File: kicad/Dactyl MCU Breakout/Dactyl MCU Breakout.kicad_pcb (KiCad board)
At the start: 4 copper layers, 48.5 x 61.1 mm, 37 parts, among them J202 Split, J203 Column, J204 Thumb, J205 External, J206 Row, J207 Display, J208 Vic, J209 JST, SW201 Battery, SW202 Reset, SW203 LED, U201 SRV05-4, U202 Nice!Nano/2040

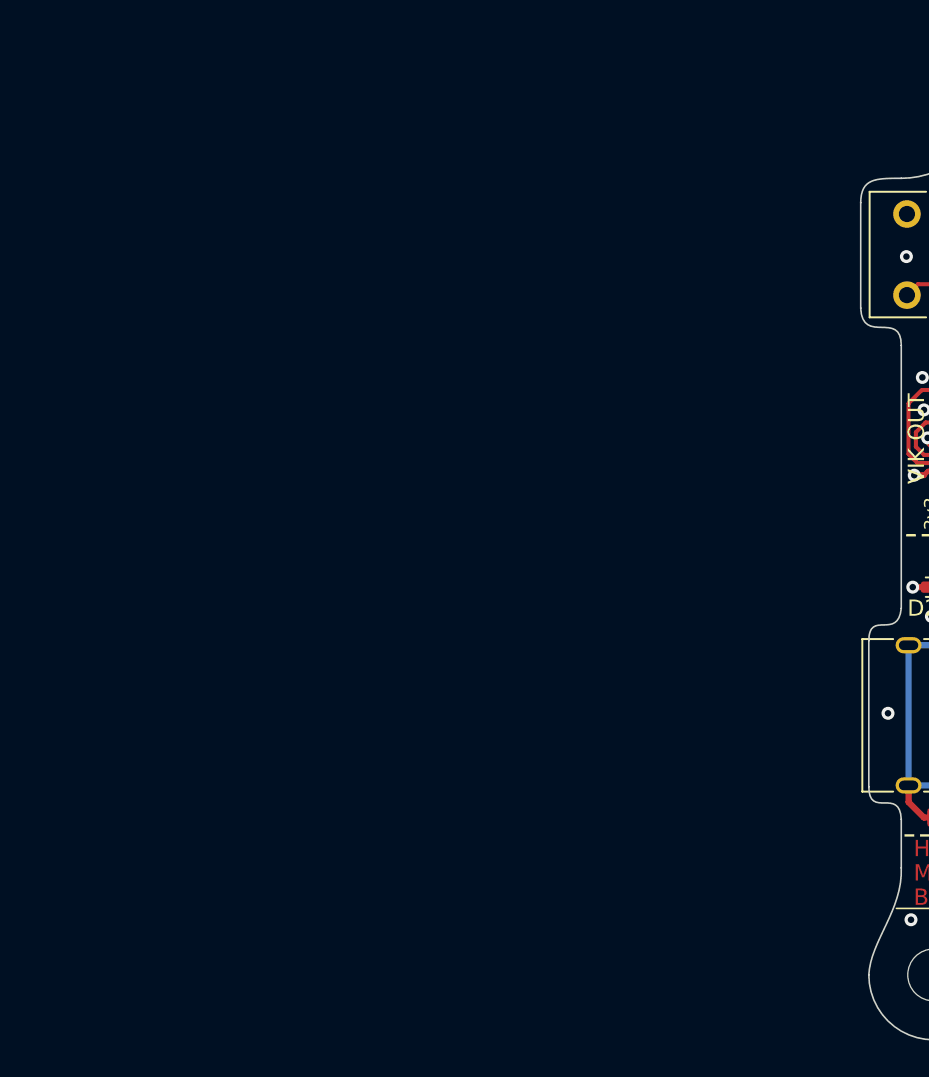
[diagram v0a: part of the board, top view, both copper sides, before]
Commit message: feat(pcb): mirror flipped
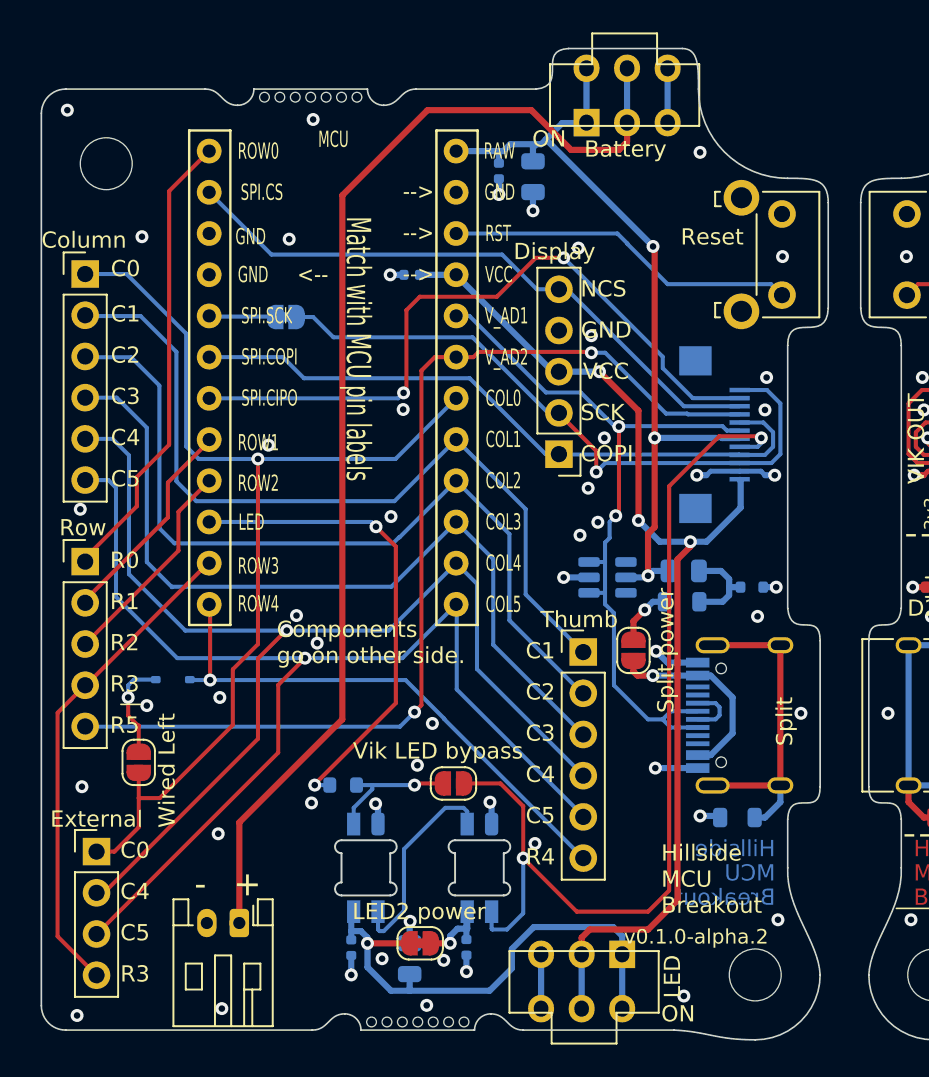
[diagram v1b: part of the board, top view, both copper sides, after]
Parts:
- added C202: 4.7uF, Capacitor_SMD:C_0805_2012Metric, B.Cu at (80.3, 55.4)
- added C203: 0.1uF, Capacitor_SMD:C_0402_1005Metric, B.Cu at (78.2, 55.0)
- added C204: 0.1uF, Capacitor_SMD:C_0402_1005Metric, B.Cu at (72.8, 61.5)
- added C205: 22uF, Capacitor_SMD:C_0805_2012Metric, B.Cu at (72.7, 103.6)
- added C206: 0.1uF, Capacitor_SMD:C_0402_1005Metric, B.Cu at (69.1, 102.9)
- added C207: 0.1uF, Capacitor_SMD:C_0402_1005Metric, B.Cu at (76.2, 102.9)
- added D201: ESD5Z5V0, Diode_SMD:D_SOD-523, B.Cu at (93.8, 80.7)
- added D202: D_Small, Diode_SMD:D_SOD-323, B.Cu at (58.1, 86.4)
- added D203: SK6812-MINI-E, Dactyl:SK6812-MINI-E-Dog2_1S, B.Cu at (70.0, 98.0)
- added D204: SK6812-MINI-E, Dactyl:SK6812-MINI-E-Dog2_1S, B.Cu at (77.0, 98.0)
- added F201: 750mA 6V Polyfuse, Fuse:Fuse_0805_2012Metric, B.Cu at (89.6, 79.7)
- added FB201: 20mΩ 100Ω@100MHz, Inductor_SMD:L_0805_2012Metric, B.Cu at (92.9, 94.9)
- added FB202: 20mΩ 100Ω@100MHz, Inductor_SMD:L_0805_2012Metric, B.Cu at (89.5, 81.6)
- added H201: MountingHole, Dactyl_basics:MountingHole_3.2mm_M3_DIN965, B.Cu at (54.0, 54.6)
- added H202: MountingHole, Dactyl_basics:MountingHole_3.2mm_M3_DIN965, B.Cu at (94.0, 104.6)
- added J202: Split, Dactyl_basics:USB_C_Receptacle_HRO_TYPE-C-31-M-12, B.Cu at (94.5, 88.6)
- added J203: Column, Dactyl:PinHeader_Columns, B.Cu at (52.7, 61.4)
- added J204: Thumb, Dactyl:PinHeader_Thumbs, B.Cu at (83.4, 84.7)
- added J205: External, Dactyl:PinHeader_External, B.Cu at (53.4, 97.0)
- added J206: Row, Dactyl:PinHeader_Rows, B.Cu at (52.7, 79.1)
- added J207: Display, Dactyl:PinHeader_Display, B.Cu at (81.9, 72.5)
- added J208: Vic, Dactyl:vik-keyboard-connector-horizontal, B.Cu at (91.0, 71.3)
- added J209: JST, Dactyl:JST_PH_S2B-PH-K_1x02_P2.00mm_Horizontal, B.Cu at (62.2, 101.4)
- added JP201: Split power, Dactyl_basics:SolderJumper-2_P1.3mm_Open_RoundedPad1.0x1.5mm, F.Cu at (86.5, 84.6)
- added JP202: Wired Left, Dactyl_basics:SolderJumper-2_P1.3mm_Open_RoundedPad1.0x1.5mm, F.Cu at (56.0, 91.5)
- added JP203: SCK term, Dactyl_basics:SolderJumper-2_P1.3mm_Bridged_RoundedPad1.0x1.5mm, B.Cu at (65.1, 64.0)
- added JP204: Vik LED bypass, Dactyl_basics:SolderJumper-2_P1.3mm_Open_RoundedPad1.0x1.5mm, F.Cu at (75.4, 92.8)
- added JP205: LED2 power, Dactyl_basics:SolderJumper-2_P1.3mm_Bridged_RoundedPad1.0x1.5mm, F.Cu at (73.3, 102.7)
- added R201: 300 Ohm, Resistor_SMD:R_0603_1608Metric, B.Cu at (68.6, 92.9)
- added REF**: art_name, Dactyl:art_name, B.Cu at (92.0, 98.4)
- added REF**: Mouse_Bites, Dactyl_basics:Mouse_Bites, B.Cu at (73.2, 107.5)
- added REF**: Mouse_Bites, Dactyl_basics:Mouse_Bites, B.Cu at (66.6, 50.5)
- added SW201: Battery, Dactyl:SW_SPDT_Battery, B.Cu at (86.1, 50.4)
- added SW202: Reset, Dactyl_basics:SW_Tactile_SKHL_Angled, B.Cu at (94.4, 60.2)
- added SW203: LED, Dactyl:SW_SPDT_JS202011AQN_wider, B.Cu at (83.3, 105.0)
- added U201: SRV05-4, Package_TO_SOT_SMD:SOT-23-6, B.Cu at (84.9, 80.1)
- added U202: Nice!Nano/2040, Dactyl:ProMicro_v2_1S, B.Cu at (68.0, 68.3)
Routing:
- net /Right/col4: track 71.4 -> 142.9 mm, vias 1 -> 2
- net /Right/col5: track 71.4 -> 142.8 mm, vias 1 -> 2
- net /Right/bat+: track 69.6 -> 139.2 mm
- net /Right/col0: track 64.5 -> 129.0 mm, vias 1 -> 2
- net /Right/VCC: track 64.1 -> 128.2 mm, vias 3 -> 6
- net /Right/row5_VIK_GP_AD2: track 63.6 -> 127.2 mm, vias 2 -> 4
- net /Right/LED_out: track 59.0 -> 118.0 mm, vias 2 -> 4
- net /Right/col2: track 50.8 -> 101.6 mm
- net /Right/col3: track 50.6 -> 101.1 mm
- net /Right/col1: track 50.2 -> 100.4 mm
- net /Right/RAW: track 48.5 -> 97.1 mm, vias 3 -> 6
- net /Right/SPLIT_VIK_GP_AD1: track 47.5 -> 95.1 mm, vias 2 -> 4
- net /Right/SPI0.CIPO: track 43.2 -> 86.3 mm, vias 2 -> 4
- net /Right/SPI0.SCK/SDA: track 41.0 -> 82.0 mm, vias 1 -> 2
- net /Right/SPI0.COPI/SCL: track 40.7 -> 81.4 mm
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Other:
- board size 48.5 x 61.1 mm -> 99 x 61.1 mm

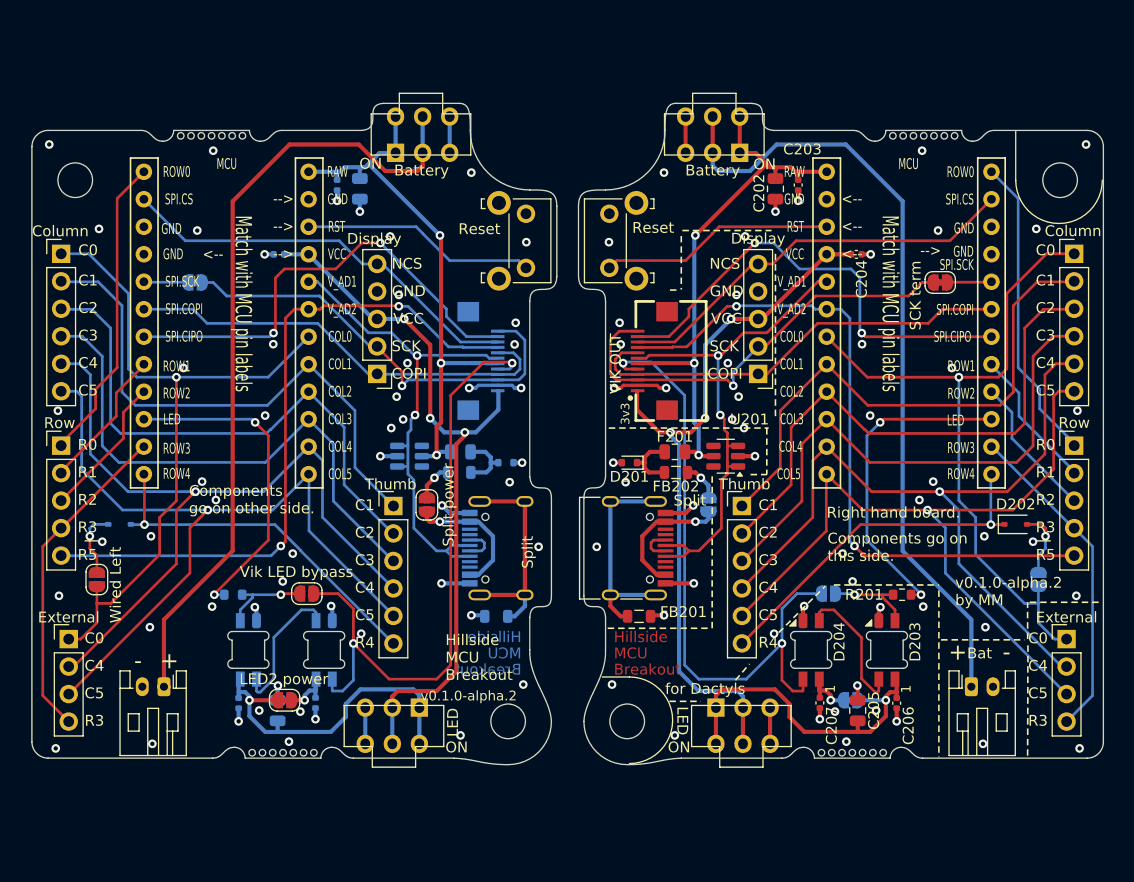
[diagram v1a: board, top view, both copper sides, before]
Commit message: feat(pcb): left half re-numbered and some routed
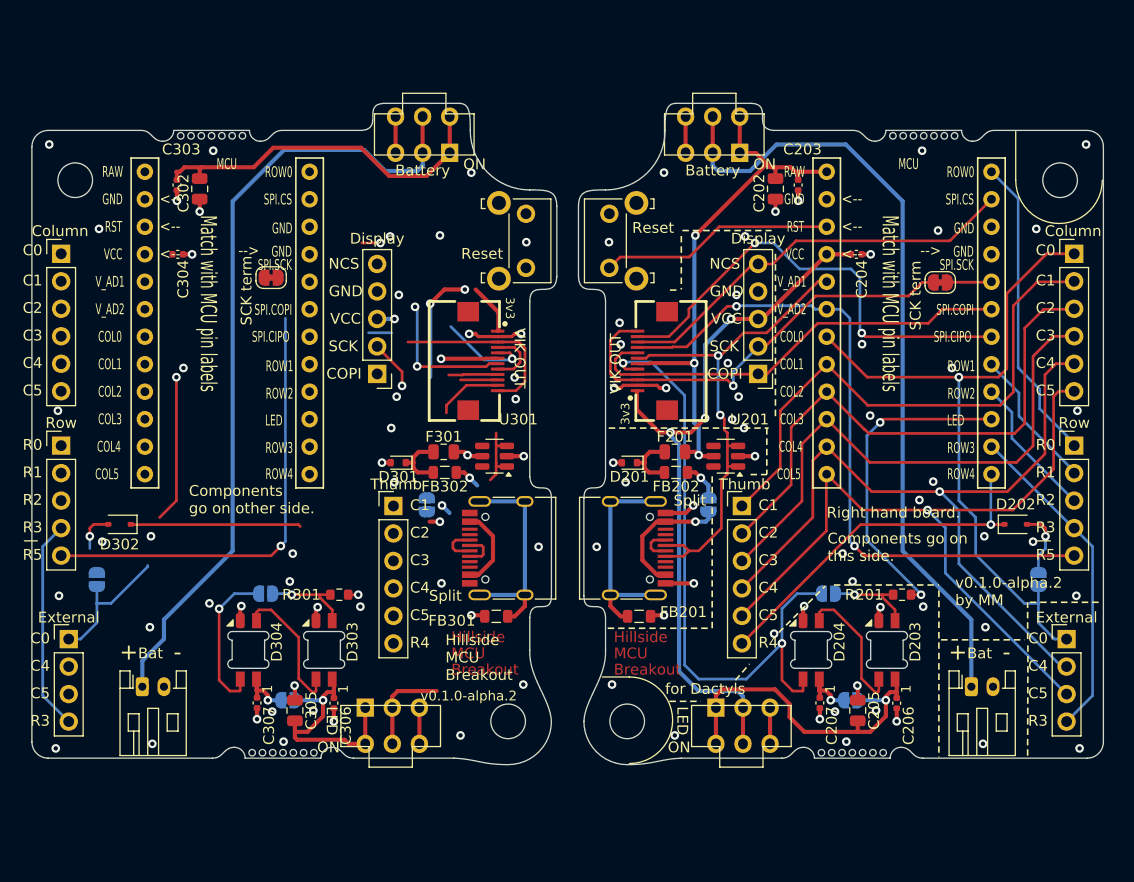
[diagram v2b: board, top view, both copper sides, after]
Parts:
- C302: renamed from C202; moved to F.Cu
- C303: renamed from C203; moved to F.Cu
- C304: renamed from C204; moved to F.Cu
- C305: renamed from C205; moved to F.Cu
- C306: renamed from C206; moved to F.Cu
- C307: renamed from C207; moved to F.Cu
- D301: renamed from D201; moved to F.Cu
- D302: renamed from D202; moved to F.Cu
- D303: renamed from D203; moved to F.Cu
- D304: renamed from D204; moved to F.Cu
- F301: renamed from F201; moved to F.Cu
- FB301: renamed from FB201; moved to F.Cu
- FB302: renamed from FB202; moved to F.Cu
- H301: renamed from H201; moved to F.Cu
- H302: renamed from H202; moved to F.Cu
- J302: renamed from J202; moved to F.Cu
- J303: renamed from J203; moved to F.Cu
- J304: renamed from J204; moved to F.Cu
- J305: renamed from J205; moved to F.Cu
- J306: renamed from J206; moved to F.Cu
- J307: renamed from J207; moved to F.Cu
- J308: renamed from J208; moved to F.Cu
- J309: renamed from J209; moved to F.Cu
- JP301: renamed from JP201; moved to B.Cu
- JP302: renamed from JP202; moved to B.Cu
- JP303: renamed from JP203; moved to F.Cu
- JP304: renamed from JP204; moved to B.Cu
- JP305: renamed from JP205; moved to B.Cu
- R301: renamed from R201; moved to F.Cu
- REF** (x3): moved to F.Cu
- SW301: renamed from SW201; moved to F.Cu
- SW302: renamed from SW202; moved to F.Cu
- SW303: renamed from SW203; moved to F.Cu
- U301: renamed from U201; moved to F.Cu
- U302: renamed from U202; moved to F.Cu
- moved C303 14.8 mm to (63.4, 55.0)
- moved C302 14.8 mm to (65.5, 55.4)
- moved D301 9.95 mm to (83.8, 80.7), turned to 180 degrees
- moved R301 9.80 mm to (78.4, 92.9), turned to 180 degrees
- moved C304 9.35 mm to (63.5, 61.5), turned to 180 degrees
- moved C306 8.80 mm to (77.9, 102.9)
- moved U301 7.85 mm to (92.7, 80.1), turned to 180 degrees
- moved JP303 7.04 mm to (72.1, 63.6), turned to 180 degrees
- moved D303 7.00 mm to (77.0, 98.0)
- moved D304 7.00 mm to (70.0, 98.0)
- moved C307 5.40 mm to (70.8, 102.9)
- moved JP304 3.80 mm to (71.6, 92.8), turned to 180 degrees
- moved J309 2.00 mm to (60.2, 101.4), turned to 0 degrees
- moved C305 1.60 mm to (74.3, 103.6)
- moved F301 1.55 mm to (88.0, 79.7), turned to 0 degrees
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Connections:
- SW301 pad 3: unconnected-(SW201-C-Pad3)_1 -> unconnected-(SW201-C-Pad3)_0
- SW303 pad 3: unconnected-(SW203-C-Pad3)_1 -> unconnected-(SW203-C-Pad3)_0
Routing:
- net /Right/col4: track 142.9 -> 71.5 mm, vias 2 -> 1
- net /Right/col5: track 142.8 -> 71.5 mm, vias 2 -> 1
- net /Right/VCC: track 128.2 -> 75.8 mm, vias 6 -> 4
- net /Right/col2: track 101.6 -> 50.8 mm
- net /Right/col3: track 101.1 -> 50.6 mm
- net /Right/col1: track 100.4 -> 50.2 mm
- net /Right/col0: track 129.0 -> 90.9 mm
- net /Right/LED_out: track 118.0 -> 82.2 mm
- net /Right/SPI0.CIPO: track 86.3 -> 51.1 mm, vias 4 -> 3
- net /Right/SPI0.COPI/SCL: track 81.4 -> 46.2 mm
- net /Right/SPI0.SC: track 76.3 -> 42.1 mm
- net /Right/LED: track 59.7 -> 30.8 mm, vias 4 -> 3
- net /Right/row0: track 56.9 -> 28.5 mm
- net /Right/RST: track 43.3 -> 21.7 mm
- net /Right/SPI0.SCK/SDA: track 82.0 -> 62.6 mm
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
